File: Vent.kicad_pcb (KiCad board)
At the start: 4 copper layers, 38.1 x 17.6 mm, 26 parts, among them J2 B2B-XH-A_LF__SN_, J3 Conn_01x03_Pin, J4 Conn_01x04_Socket, SW1 SW_Push, U1 ESP32-H2-MINI-1, U4 MCP1640x-xMC

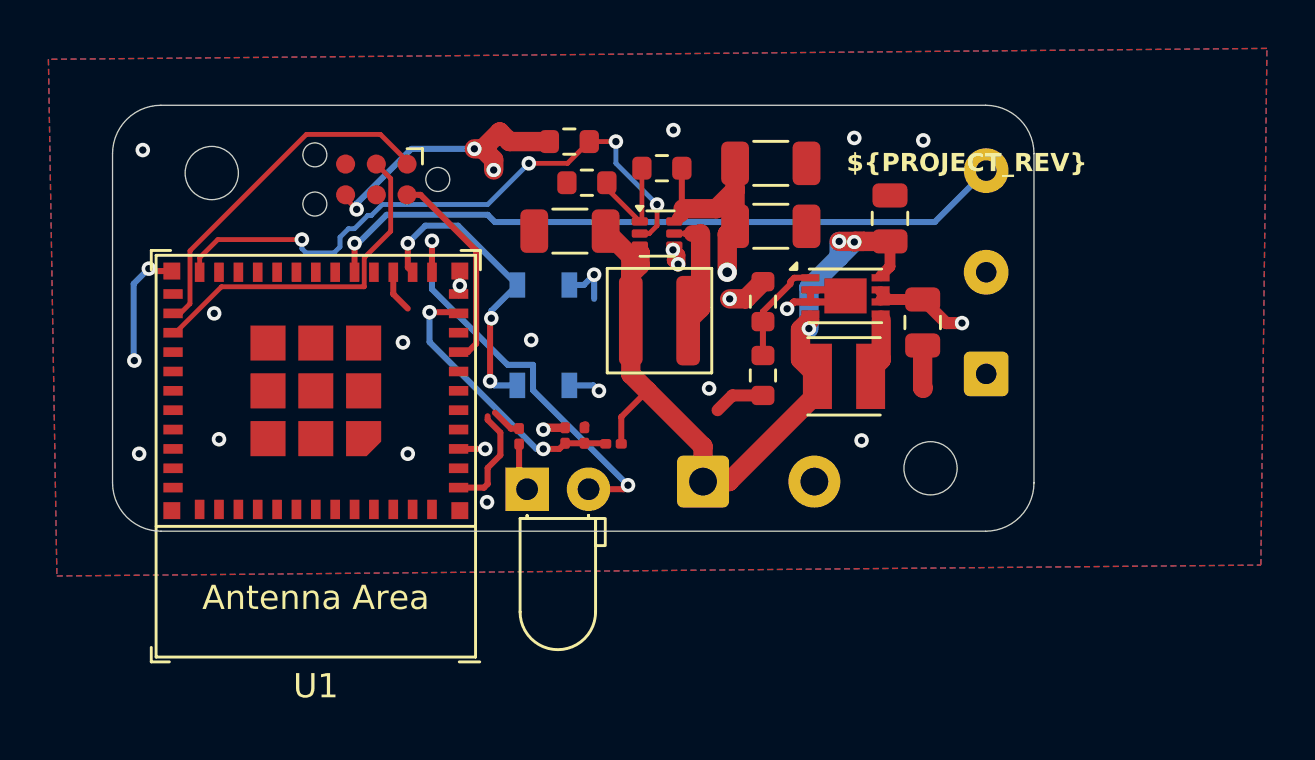
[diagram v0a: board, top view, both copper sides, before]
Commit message: feat: Disconnect EN pin from external autoprogramming
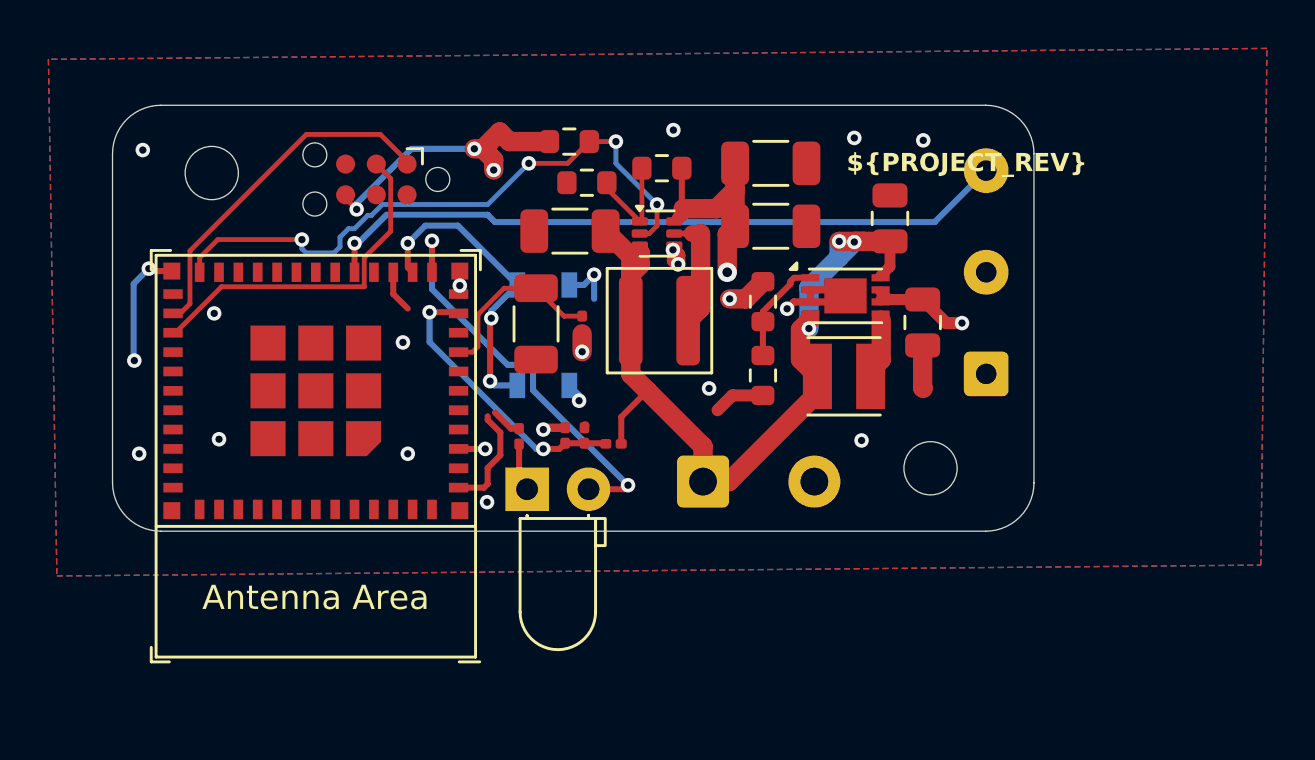
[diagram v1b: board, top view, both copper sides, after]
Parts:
- added C4: 1uF, Capacitor_SMD:C_1206_3216Metric, F.Cu at (139.7, 68.8)
- added R4: 10k, Resistor_SMD:R_0201_0603Metric, F.Cu at (141.6, 68.8)
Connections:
- J4 pad 2: /EN -> unconnected-(J4-EN-Pad2)
- U1 pad 8: /EN -> Net-(U1-EN)
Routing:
- net /EN: track 8.53 -> 0.00 mm
- net Net-(U1-EN): track 0.00 -> 7.45 mm
- net +3.3V: track 32.9 -> 33.7 mm, vias 3 -> 4
- net GND: track 40.1 -> 39.5 mm, vias 25 -> 24

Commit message: feat: Replace autoprogramming symbol with Conn_02x03
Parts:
- J4: value Conn_01x04_Socket -> Conn_02x03_Odd_Even
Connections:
- J4 pad 5: unconnected-(J4-VCC-Pad5) -> GND
- J4 pad 6: GND -> unconnected-(J4-Pin_6-Pad6)
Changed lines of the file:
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@@
 			)
 		)
-		(property "Value" "Conn_01x04_Socket"
+		(property "Value" "Conn_02x03_Odd_Even"
 			(at 0 -2.3 0)
 			(layer "F.Fab")
@@
 			(layers "F.Cu" "F.Mask")
 			(net "/D-")
-			(pinfunction "D-_1")
-			(pintype "bidirectional")
+			(pinfunction "Pin_1_1")
+			(pintype "passive")
 		)
 		(pad "2" connect circle
@@
 			(size 0.7874 0.7874)
 			(layers "F.Cu" "F.Mask")
-			(net "unconnected-(J4-EN-Pad2)")
-			(pinfunction "EN_2")
-			(pintype "input+no_connect")
+			(net "unconnected-(J4-Pin_2-Pad2)")
+			(pinfunction "Pin_2_2")
+			(pintype "passive+no_connect")
 		)
 		(pad "3" connect circle
@@
 			(layers "F.Cu" "F.Mask")
 			(net "/D+")
-			(pinfunction "D+_3")
-			(pintype "bidirectional")
+			(pinfunction "Pin_3_3")
+			(pintype "passive")
 		)
 		(pad "4" connect circle
@@
 			(size 0.7874 0.7874)
 			(layers "F.Cu" "F.Mask")
-			(net "unconnected-(J4-BOOT-Pad4)")
-			(pinfunction "BOOT_4")
-			(pintype "bidirectional+no_connect")
+			(net "unconnected-(J4-Pin_4-Pad4)")
+			(pinfunction "Pin_4_4")
+			(pintype "passive+no_connect")
 		)
 		(pad "5" connect circle
@@
 			(size 0.7874 0.7874)
 			(layers "F.Cu" "F.Mask")
-			(net "unconnected-(J4-VCC-Pad5)")
-			(pinfunction "VCC_5")
-			(pintype "power_out+no_connect")
+			(net "GND")
+			(pinfunction "Pin_5_5")
+			(pintype "passive")
 		)
 		(pad "6" connect circle
@@
 			(size 0.7874 0.7874)
 			(layers "F.Cu" "F.Mask")
-			(net "GND")
-			(pinfunction "GND_6")
-			(pintype "power_out")
+			(net "unconnected-(J4-Pin_6-Pad6)")
+			(pinfunction "Pin_6_6")
+			(pintype "passive+no_connect")
 		)
 		(zone
@@
 	)
 	(segment
-		(start 131.83 63.645334)
-		(end 131.83 63.5)
-		(width 0.2)
-		(layer "F.Cu")
-		(net "GND")
-	)
-	(segment
 		(start 137.7 75.45)
 		(end 137.7 74.785298)
@@
 	)
 	(segment
-		(start 132.287552 64.102886)
-		(end 131.83 63.645334)
-		(width 0.2)
-		(layer "F.Cu")
-		(net "GND")
-	)
-	(segment
 		(start 145.57061 65.988383)
 		(end 145.357227 65.775)
@@
 	)
 	(segment
+		(start 131.83 62.23)
+		(end 131.322 62.738)
+		(width 0.2)
+		(layer "F.Cu")
+		(net "GND")
+	)
+	(segment
 		(start 137.5 61.6)
 		(end 138.2 60.9)
@@
 		(end 145.4125 65.652941)
 		(width 0.25)
+		(layer "F.Cu")
+		(net "GND")
+	)
+	(segment
+		(start 131.322 62.738)
+		(end 130.81 62.738)
+		(width 0.2)
 		(layer "F.Cu")
 		(net "GND")
@@
 	)
 	(via
-		(at 132.287552 64.102886)
+		(at 129.921 62.865)
 		(size 0.6)
 		(drill 0.3)
